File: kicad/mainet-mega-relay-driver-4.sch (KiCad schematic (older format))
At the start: 8 parts, among them J33 Screw_Terminal_01x03, K4 SANYOU_SRD_Form_C, Q4 2N3904, U5 4N37

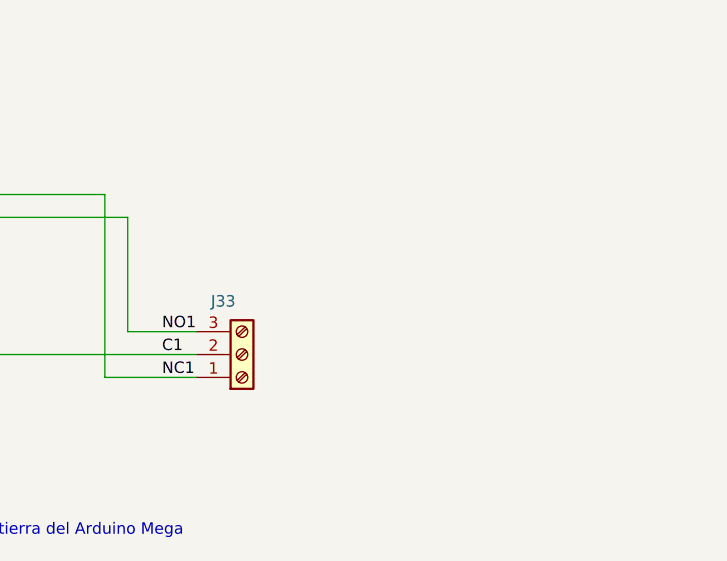
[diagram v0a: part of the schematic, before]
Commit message: KICAD: Actualizar esquemáticos
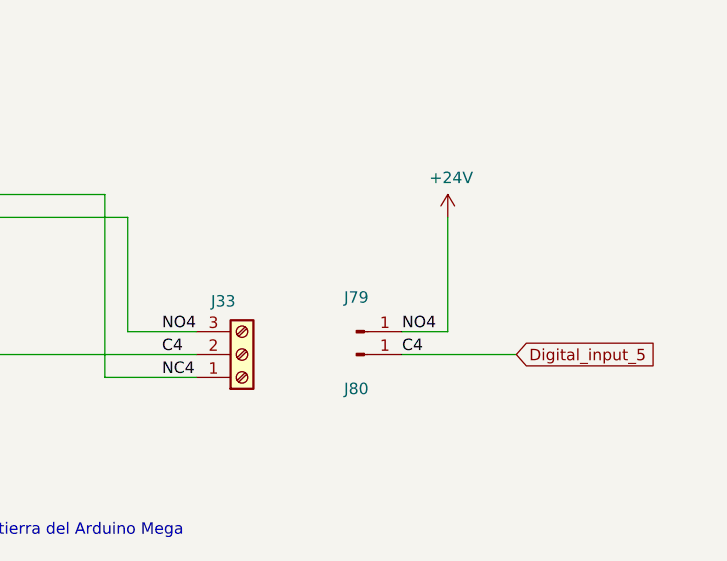
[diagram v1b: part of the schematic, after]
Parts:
- added J79, J80: Conn_01x01_Male, symbol Connector:Conn_01x01_Male
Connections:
- net C1 renamed Digital_input_5
- net Digital_input_5: now also J80.1 (Pin_1)
- net NC1 renamed NC4
- net NO1 renamed +24V
- net +24V: now also J79.1 (Pin_1)
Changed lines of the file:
@@
 encoding utf-8
 Sheet 10 21
-Title "Mainet-mega -- "
-Date "2021-04-06"
+Title "Mainet-mega -- analogInputSelectControl"
+Date "2021-04-07"
 Rev "1.0"
 Comp "Tovenca"
@@
 	7600 3900 8000 3900
 Text Label 7850 3700 0    50   ~ 0
-NO1
+NO4
 Text Label 7850 3800 0    50   ~ 0
-C1
+C4
 Text Label 7850 3900 0    50   ~ 0
-NC1
+NC4
 Wire Wire Line
 	8000 3700 7700 3700
@@
 Text Notes 3550 4350 0    50   ~ 0
 D18-analogInputSelectControl
+$Comp
+L Connector:Conn_01x01_Male J?
+U 1 1 606FB823
+P 8700 3700
+AR Path="/5FC25793/5FD90A95/606FB823" Ref="J?"  Part="1"
+AR Path="/5FC25793/5FD91471/606FB823" Ref="J79"  Part="1"
+F 0 "J79" H 8700 3850 50  0000 C CNN
+F 1 "Conn_01x01_Male" H 8808 3790 50  0001 C CNN
+F 2 "" H 8700 3700 50  0001 C CNN
+F 3 "~" H 8700 3700 50  0001 C CNN
+	1    8700 3700
+	1    0    0    -1
+$EndComp
+$Comp
+L Connector:Conn_01x01_Male J?
+U 1 1 606FB829
+P 8700 3800
+AR Path="/5FC25793/5FD90A95/606FB829" Ref="J?"  Part="1"
+AR Path="/5FC25793/5FD91471/606FB829" Ref="J80"  Part="1"
+F 0 "J80" H 8700 3650 50  0000 C CNN
+F 1 "Conn_01x01_Male" H 8808 3890 50  0001 C CNN
+F 2 "" H 8700 3800 50  0001 C CNN
+F 3 "~" H 8700 3800 50  0001 C CNN
+	1    8700 3800
+	1    0    0    -1
+$EndComp
+$Comp
+L power:+24V #PWR?
+U 1 1 606FB82F
+P 9100 3200
+AR Path="/5FC25793/5FD90A95/606FB82F" Ref="#PWR?"  Part="1"
+AR Path="/5FC25793/5FD91471/606FB82F" Ref="#PWR043"  Part="1"
+F 0 "#PWR043" H 9100 3050 50  0001 C CNN
+F 1 "+24V" H 9115 3373 50  0000 C CNN
+F 2 "" H 9100 3200 50  0001 C CNN
+F 3 "" H 9100 3200 50  0001 C CNN
+	1    9100 3200
+	1    0    0    -1
+$EndComp
+Wire Wire Line
+	9100 3200 9100 3700
+Wire Wire Line
+	9100 3700 8900 3700
+Text Label 8900 3700 0    50   ~ 0
+NO4
+Text Label 8900 3800 0    50   ~ 0
+C4
+Wire Wire Line
+	8900 3800 9400 3800
+Text GLabel 9400 3800 2    50   Input ~ 0
+Digital_input_5
 $EndSCHEMATC

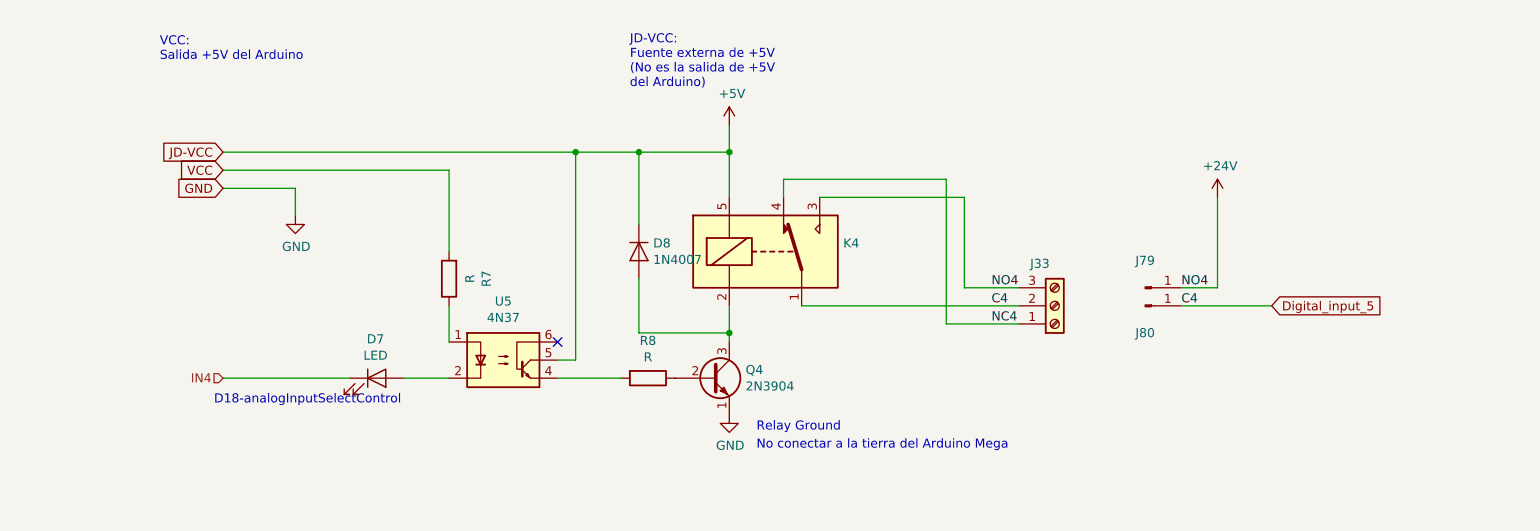
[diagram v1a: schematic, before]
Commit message: KICAD: Modificar esquemático
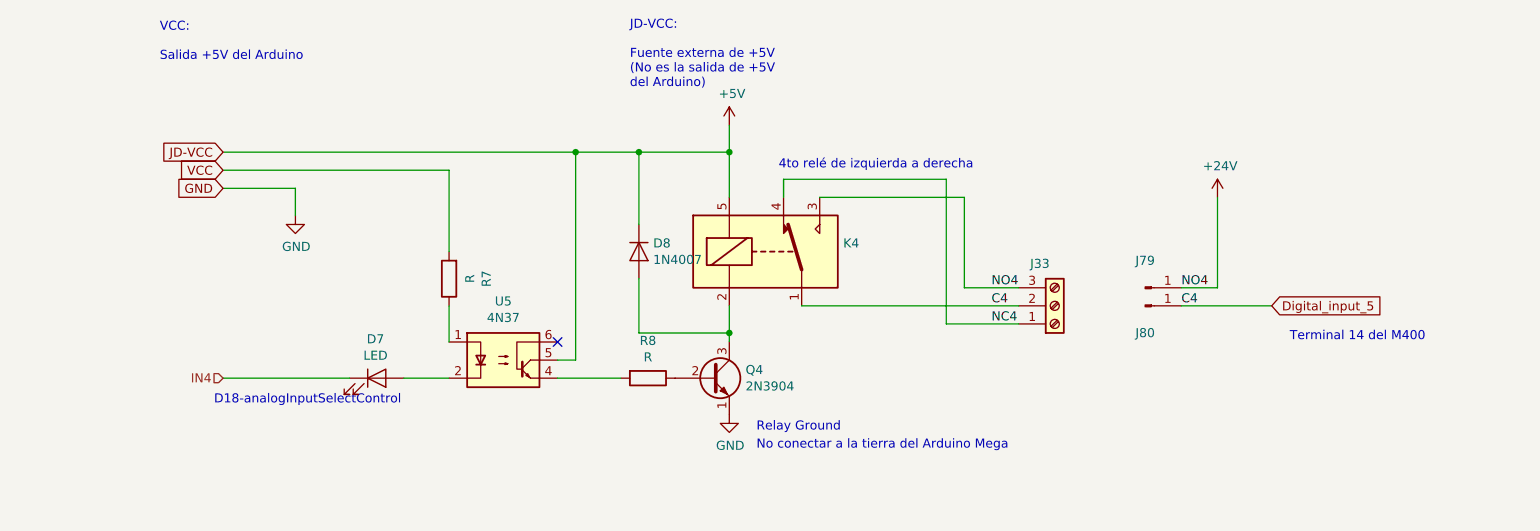
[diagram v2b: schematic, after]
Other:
- note added: "4to relé de izquierda a derecha"
- note added: "JD-VCC:\n\nFuente externa de +5V\n(No es la salida de +5V \ndel Arduino)"
- note added: "Terminal 14 del M400"
- note added: "VCC:\n\nSalida +5V del Arduino"
- note removed: "JD-VCC:\nFuente externa de +5V\n(No es la salida de +5V \ndel Arduino)"
- note removed: "VCC:\nSalida +5V del Arduino"
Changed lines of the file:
@@
 EESchema Schematic File Version 4
+LIBS:mainet-mega-cache
 EELAYER 30 0
 EELAYER END
@@
 GND
 Text Notes 5850 2600 0    50   ~ 0
-JD-VCC:\nFuente externa de +5V\n(No es la salida de +5V \ndel Arduino)
+JD-VCC:\n\nFuente externa de +5V\n(No es la salida de +5V \ndel Arduino)
 Text Notes 3250 2450 0    50   ~ 0
-VCC:\nSalida +5V del Arduino
+VCC:\n\nSalida +5V del Arduino
 Text Notes 3550 4350 0    50   ~ 0
 D18-analogInputSelectControl
@@
 Text GLabel 9400 3800 2    50   Input ~ 0
 Digital_input_5
+Text Notes 10250 4000 2    50   ~ 0
+Terminal 14 del M400
+Text Notes 7750 3050 2    50   ~ 0
+4to relé de izquierda a derecha
 $EndSCHEMATC

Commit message: KICAD: Actualizar archivos del módulo de relés
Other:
- note added: "Relay Ground\nNo conectar a la tierra\ndel Arduino Mega\n"
- note removed: "No conectar a la tierra del Arduino Mega\n"
- note removed: "Relay Ground\n"
- moved on the sheet: D7, D8, J33, J79, J80, K4, Q4, R7, R8, U5

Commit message: KICAD: Agregar cambios esquemáticos
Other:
- note added: "Nota:\nEsta tensión de 24V la proporciona el M400, \nen los terminales 9 y 17."
- note added: "Terminal 9 del M400"
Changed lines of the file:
@@
 $EndComp
 Wire Wire Line
-	8400 3250 8400 3750
+	8400 3250 8400 3300
 Wire Wire Line
 	8400 3750 8200 3750
@@
 Text Notes 5350 4950 0    50   ~ 0
 Relay Ground\nNo conectar a la tierra\ndel Arduino Mega\n
+Text GLabel 8700 3300 2    50   Input ~ 0
+24V_user
+Wire Wire Line
+	8400 3300 8700 3300
+Text Notes 8700 3450 0    50   ~ 0
+Terminal 9 del M400
+Text Notes 8700 3700 0    50   ~ 0
+Nota:\nEsta tensión de 24V la proporciona el M400, \nen los terminales 9 y 17.
+Connection ~ 8400 3300
+Wire Wire Line
+	8400 3300 8400 3750
 $EndSCHEMATC
